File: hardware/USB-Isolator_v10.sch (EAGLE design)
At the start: 33 parts, among them IC1 ADUM3160, J1 USB-MICRO, J2 USB-A-AUY1006, U1A RI-0505S, U1B SPU02L-05, X1 PASSER-07, X2 PASSER-07, X3 PASSER-07

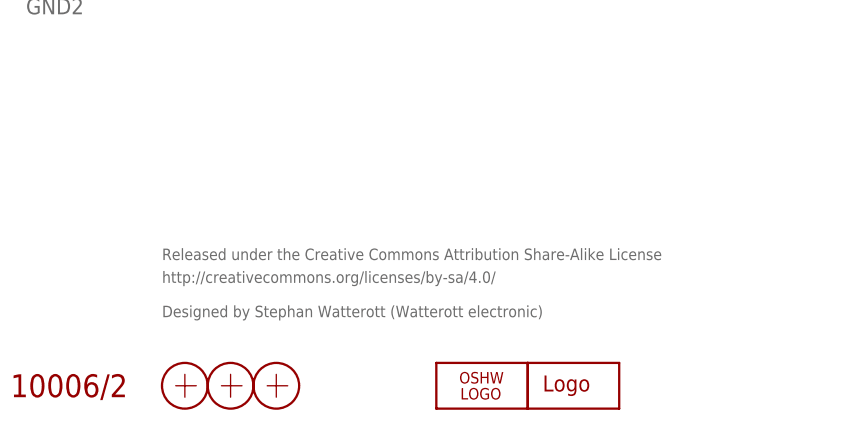
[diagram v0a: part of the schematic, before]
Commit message: updated schematics
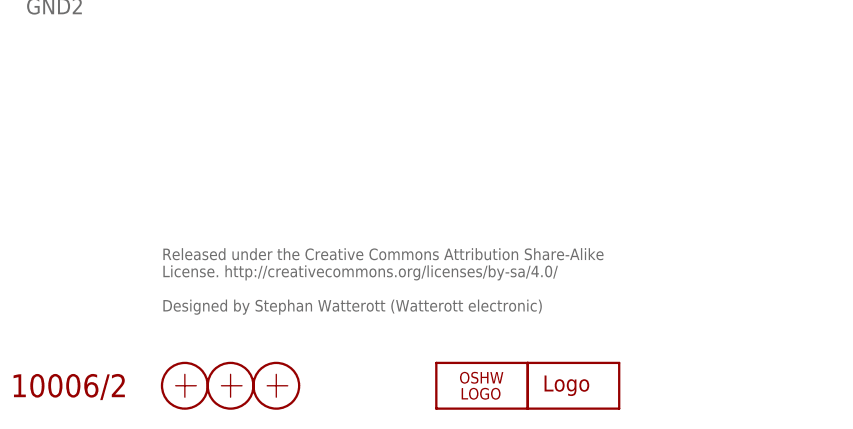
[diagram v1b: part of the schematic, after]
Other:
- note added: "Released under the Creative Commons Attribution Share-Alike License. http://creativecommons.org/licenses/by-sa/4.0/ Designed by Stephan Watterott (Watterott electronic)"
- note removed: "Designed by Stephan Watterott (Watterott electronic)"
- note removed: "Released under the Creative Commons Attribution Share-Alike License"
- note removed: "http://creativecommons.org/licenses/by-sa/4.0/"
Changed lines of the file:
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@@
 <?xml version="1.0" encoding="utf-8"?>
 <!DOCTYPE eagle SYSTEM "eagle.dtd">
-<eagle version="7.2.0">
+<eagle version="7.5.0">
 <drawing>
 <settings>
@@
 <setting verticaltext="up"/>
 </settings>
-<grid distance="0.1" unitdist="inch" unit="inch" style="lines" multiple="1" display="no" altdistance="0.01" altunitdist="inch" altunit="inch"/>
+<grid distance="0.05" unitdist="inch" unit="inch" style="lines" multiple="1" display="yes" altdistance="0.025" altunitdist="inch" altunit="inch"/>
 <layers>
 <layer number="1" name="Top" color="4" fill="1" visible="no" active="no"/>
@@
 <layer number="51" name="tDocu" color="7" fill="1" visible="no" active="no"/>
 <layer number="52" name="bDocu" color="7" fill="1" visible="no" active="no"/>
-<layer number="53" name="tGND_GNDA" color="7" fill="9" visible="no" active="no"/>
-<layer number="54" name="bGND_GNDA" color="1" fill="9" visible="no" active="no"/>
-<layer number="56" name="wert" color="7" fill="1" visible="no" active="no"/>
-<layer number="57" name="tCAD" color="7" fill="1" visible="no" active="no"/>
 <layer number="91" name="Nets" color="2" fill="1" visible="yes" active="yes"/>
 <layer number="92" name="Busses" color="1" fill="1" visible="yes" active="yes"/>
@@
 <layer number="98" name="Guide" color="6" fill="1" visible="yes" active="yes"/>
 <layer number="99" name="SpiceOrder" color="5" fill="1" visible="yes" active="yes"/>
-<layer number="100" name="Muster" color="7" fill="1" visible="no" active="no"/>
-<layer number="153" name="FabDoc1" color="6" fill="1" visible="no" active="no"/>
-<layer number="154" name="FabDoc2" color="2" fill="1" visible="no" active="no"/>
-<layer number="155" name="FabDoc3" color="7" fill="15" visible="no" active="no"/>
-<layer number="217" name="217bmp" color="18" fill="1" visible="no" active="no"/>
-<layer number="218" name="218bmp" color="19" fill="1" visible="no" active="no"/>
-<layer number="219" name="219bmp" color="20" fill="1" visible="no" active="no"/>
-<layer number="220" name="220bmp" color="21" fill="1" visible="no" active="no"/>
-<layer number="221" name="221bmp" color="22" fill="1" visible="no" active="no"/>
-<layer number="222" name="222bmp" color="23" fill="1" visible="no" active="no"/>
-<layer number="223" name="223bmp" color="24" fill="1" visible="no" active="no"/>
-<layer number="224" name="224bmp" color="25" fill="1" visible="no" active="no"/>
-<layer number="250" name="Descript" color="3" fill="1" visible="no" active="no"/>
-<layer number="251" name="SMDround" color="12" fill="11" visible="no" active="no"/>
 </layers>
 <schematic xreflabel="%F%N/%S.%C%R" xrefpart="/%S.%C%R">
@@
 <plain>
 <text x="158.75" y="8.89" size="2.54" layer="94" rot="R180">Suitable Case: Teko SOAP 1 10006/2</text>
-<text x="162.56" y="21.59" size="1.27" layer="95">Released under the Creative Commons Attribution Share-Alike License</text>
-<text x="162.56" y="19.05" size="1.27" layer="95">http://creativecommons.org/licenses/by-sa/4.0/</text>
-<text x="162.56" y="15.24" size="1.27" layer="95">Designed by Stephan Watterott (Watterott electronic)</text>
+<text x="162.56" y="22.86" size="1.27" layer="95" align="top-left">Released under the Creative Commons Attribution Share-Alike
+License. http://creativecommons.org/licenses/by-sa/4.0/
+Designed by Stephan Watterott (Watterott electronic) </text>
 <text x="107.95" y="91.44" size="3.81" layer="94">DC/DC Converter</text>
 <text x="114.3" y="151.13" size="3.81" layer="94">USB Isolator</text>

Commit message: updated layout and schematics
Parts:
- L1: value LED-0603 -> red
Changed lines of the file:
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@@
 <setting verticaltext="up"/>
 </settings>
-<grid distance="0.05" unitdist="inch" unit="inch" style="lines" multiple="1" display="yes" altdistance="0.025" altunitdist="inch" altunit="inch"/>
+<grid distance="0.1" unitdist="inch" unit="inch" style="lines" multiple="1" display="no" altdistance="0.01" altunitdist="inch" altunit="inch"/>
 <layers>
 <layer number="1" name="Top" color="4" fill="1" visible="no" active="no"/>
@@
 <part name="X1" library="we-symbol" deviceset="PASSER" device="-07"/>
 <part name="X2" library="we-symbol" deviceset="PASSER" device="-07"/>
-<part name="L1" library="we-opto" deviceset="LED" device="-0603"/>
+<part name="L1" library="we-opto" deviceset="LED" device="-0603" value="red"/>
 <part name="R5" library="we-rcl" deviceset="RESISTOR" device="-R0603" value="1k"/>
 <part name="GND7" library="supply2" deviceset="GND1" device=""/>
